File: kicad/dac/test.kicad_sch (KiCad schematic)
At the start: 9 parts, among them U1 PCM2704/4C/5/5C, Y1 12MHz±0.05%

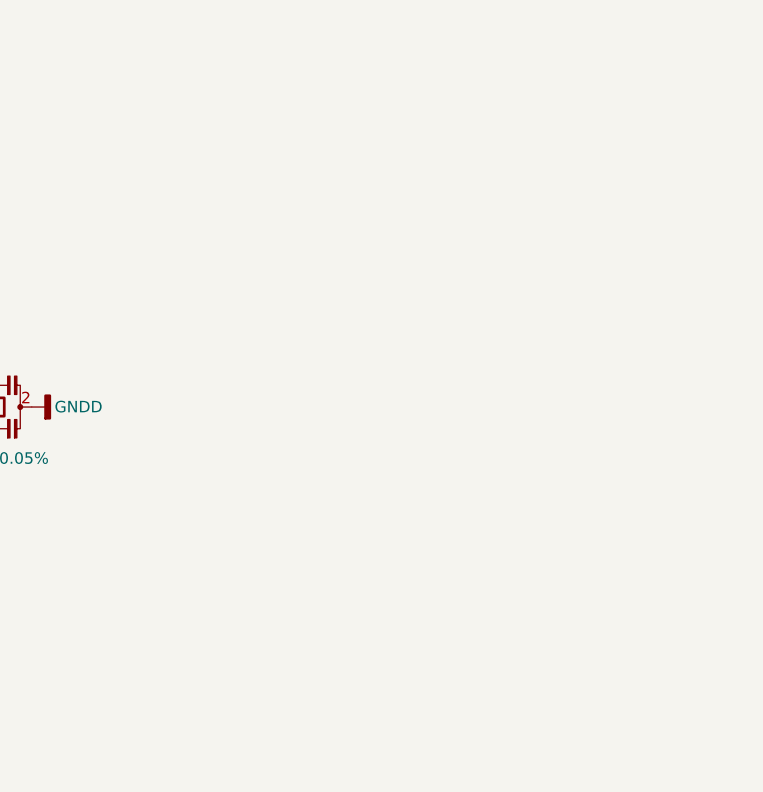
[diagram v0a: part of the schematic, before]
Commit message: completed power supply footprints and placement
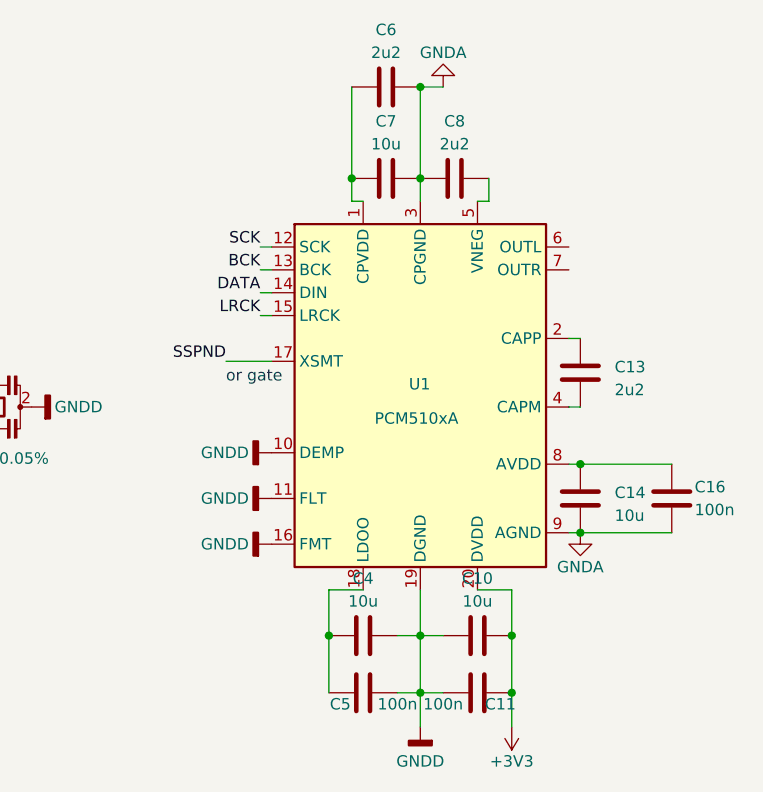
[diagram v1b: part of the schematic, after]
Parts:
- added C10, C14, C4, C7: 10u, Capacitor_SMD:C_1206_3216Metric_Pad1.33x1.80mm_HandSolder, symbol Device:C
- added C11, C16, C5: 100n, Capacitor_SMD:C_1206_3216Metric_Pad1.33x1.80mm_HandSolder, symbol Device:C
- added C13, C6, C8: 2u2, Capacitor_SMD:C_1206_3216Metric_Pad1.33x1.80mm_HandSolder, symbol Device:C
- added U1: PCM510xA, Package_SO:TSSOP-20_4.4x6.5mm_P0.65mm, symbol library:PCM510xA
- C2, C3, C4, C5, C6, R13, R14, U1, Y1: now left out of the parts list
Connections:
- net GNDA: now also C14.2, C16.2, C6.2, C7.2, C8.1, U1.3 (CPGND), U1.9 (AGND)
- net GNDD: now also C10.1, C11.1, C4.2, C5.1, U1.10 (DEMP), U1.11 (FLT), U1.16 (FMT), U1.19 (DGND)
- new net: C6.1, C7.1, U1.1 (CPVDD)
- new net: C4.1, C5.2, U1.18 (LDOO)
- new net: C13.1, U1.2 (CAPP)
- new net: C13.2, U1.4 (CAPM)
- new net: C14.1, C16.1, U1.8 (AVDD)
- new net: C8.2, U1.5 (VNEG)
- new net +3V3: C10.2, C11.2, U1.20 (DVDD)
- new net BCK: U1.13 (BCK)
- new net DATA: U1.14 (DIN)
- new net LRCK: U1.15 (LRCK)
- new net SCK: U1.12 (SCK)
- new net SSPND: U1.17 (XSMT)
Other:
- note added: "or gate"
- company: (none) -> Author: Jona Heinke
- title: (none) -> Test

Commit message: commit
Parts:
- added C34: 10u, symbol Device:C
- added Q11: MMBT5401, Package_TO_SOT_SMD:SOT-23-3, symbol Device:Q_PNP_BEC
- added Q6: MMBT5551, Package_TO_SOT_SMD:SOT-23-3, symbol Device:Q_NPN_BEC
- C10, C11, C13, C14, C16, C2, C3, C4, C5, C6, C7, C8, R13, R14, U1, Y1: now not fitted
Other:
- note added: "cap sizes left to buy: 33p etc. 1u 3u3 good 3u3 470u 2m2"

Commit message: commit
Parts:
- added J4: AudioJack3, symbol Connector_Audio:AudioJack3_Switch
- renumbered C34 to C35
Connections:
- no-connect marks 3 -> 9
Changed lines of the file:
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@@
   (title_block
     (title "Test")
-    (date "2023-05-25")
+    (date "2023-06-03")
     (rev "1")
     (company "Author: Jona Heinke")
@@
   )
   (no_connect (at 36.83 52.07))
+  (no_connect (at 127 127))
   (no_connect (at 72.39 46.99))
+  (no_connect (at 127 121.92))
+  (no_connect (at 127 134.62))
+  (no_connect (at 127 124.46))
+  (no_connect (at 127 129.54))
+  (no_connect (at 127 132.08))
   (no_connect (at 36.83 44.45))
   (wire (pts (xy 31.75 46.99) (xy 36.83 46.99))
@@
         )
         (path "/8a133d32-893e-4939-a0f4-ae81724d72bd/9aaf1754-900d-4340-bdec-8cf556dd71c2"
-          (reference "C43") (unit 1)
+          (reference "C44") (unit 1)
         )
       )
@@
         )
         (path "/8a133d32-893e-4939-a0f4-ae81724d72bd/9aaf1754-900d-4340-bdec-8cf556dd71c2"
-          (reference "C42") (unit 1)
+          (reference "C43") (unit 1)
         )
       )
@@
         )
         (path "/8a133d32-893e-4939-a0f4-ae81724d72bd/9aaf1754-900d-4340-bdec-8cf556dd71c2"
-          (reference "C39") (unit 1)
+          (reference "C40") (unit 1)
         )
       )
@@
         )
         (path "/8a133d32-893e-4939-a0f4-ae81724d72bd/9aaf1754-900d-4340-bdec-8cf556dd71c2"
-          (reference "C41") (unit 1)
+          (reference "C42") (unit 1)
         )
       )
@@
   (symbol (lib_id "Device:C") (at 25.4 134.62 0) (unit 1)
     (in_bom yes) (on_board yes) (dnp no) (fields_autoplaced)
-    (property "Reference" "C34" (at 29.21 133.985 0)
+    (property "Reference" "C35" (at 29.21 133.985 0)
       (effects (font (size 1.27 1.27)) (justify left))
     )
@@
       (project "dac"
         (path "/8a133d32-893e-4939-a0f4-ae81724d72bd/9aaf1754-900d-4340-bdec-8cf556dd71c2"
-          (reference "C34") (unit 1)
+          (reference "C35") (unit 1)
         )
       )
@@
         )
         (path "/8a133d32-893e-4939-a0f4-ae81724d72bd/9aaf1754-900d-4340-bdec-8cf556dd71c2"
-          (reference "C36") (unit 1)
+          (reference "C37") (unit 1)
         )
       )
@@
         )
         (path "/8a133d32-893e-4939-a0f4-ae81724d72bd/9aaf1754-900d-4340-bdec-8cf556dd71c2"
-          (reference "C47") (unit 1)
+          (reference "C48") (unit 1)
         )
       )
@@
         )
         (path "/8a133d32-893e-4939-a0f4-ae81724d72bd/9aaf1754-900d-4340-bdec-8cf556dd71c2"
-          (reference "C38") (unit 1)
+          (reference "C39") (unit 1)
         )
       )
@@
         )
         (path "/8a133d32-893e-4939-a0f4-ae81724d72bd/9aaf1754-900d-4340-bdec-8cf556dd71c2"
-          (reference "C35") (unit 1)
+          (reference "C36") (unit 1)
         )
       )
@@
         )
         (path "/8a133d32-893e-4939-a0f4-ae81724d72bd/9aaf1754-900d-4340-bdec-8cf556dd71c2"
-          (reference "C48") (unit 1)
+          (reference "C49") (unit 1)
         )
       )
@@
     )
   )
+  (symbol (lib_id "Connector_Audio:AudioJack3_Switch") (at 132.08 129.54 180) (unit 1)
+    (in_bom no) (on_board no) (dnp yes)
+    (property "Reference" "J4" (at 132.08 140.97 0)
+      (effects (font (size 1.27 1.27)))
+    )
+    (property "Value" "AudioJack3" (at 132.08 138.43 0)
+      (effects (font (size 1.27 1.27)))
+    )
+    (property "Footprint" "" (at 132.08 129.54 0)
+      (effects (font (size 1.27 1.27)) hide)
+    )
+    (property "Datasheet" "https://www.cuidevices.com/product/resource/sj-6307.pdf" (at 132.08 129.54 0)
+      (effects (font (size 1.27 1.27)) hide)
+    )
+    (property "Digikey" "2223-SJ-63073E-ND" (at 132.08 129.54 0)
+      (effects (font (size 1.27 1.27)) hide)
+    )
+    (pin "R")
+    (pin "RN")
+    (pin "S")
+    (pin "SN")
+    (pin "T")
+    (pin "TN")
+    (instances
+      (project "dac"
+        (path "/8a133d32-893e-4939-a0f4-ae81724d72bd"
+          (reference "J4") (unit 1)
+        )
+        (path "/8a133d32-893e-4939-a0f4-ae81724d72bd/9aaf1754-900d-4340-bdec-8cf556dd71c2"
+          (reference "J5") (unit 1)
+        )
+      )
+    )
+  )
   (symbol (lib_id "Device:R") (at 31.75 38.1 180) (unit 1)
     (in_bom no) (on_board no) (dnp yes) (fields_autoplaced)
@@
         )
         (path "/8a133d32-893e-4939-a0f4-ae81724d72bd/9aaf1754-900d-4340-bdec-8cf556dd71c2"
-          (reference "R61") (unit 1)
+          (reference "R65") (unit 1)
         )
       )
@@
         )
         (path "/8a133d32-893e-4939-a0f4-ae81724d72bd/9aaf1754-900d-4340-bdec-8cf556dd71c2"
-          (reference "C46") (unit 1)
+          (reference "C47") (unit 1)
         )
       )
@@
         )
         (path "/8a133d32-893e-4939-a0f4-ae81724d72bd/9aaf1754-900d-4340-bdec-8cf556dd71c2"
-          (reference "C49") (unit 1)
+          (reference "C50") (unit 1)
         )
       )
@@
         )
         (path "/8a133d32-893e-4939-a0f4-ae81724d72bd/9aaf1754-900d-4340-bdec-8cf556dd71c2"
-          (reference "C40") (unit 1)
+          (reference "C41") (unit 1)
         )
       )
@@
         )
         (path "/8a133d32-893e-4939-a0f4-ae81724d72bd/9aaf1754-900d-4340-bdec-8cf556dd71c2"
-          (reference "C44") (unit 1)
+          (reference "C45") (unit 1)
         )
       )
@@
         )
         (path "/8a133d32-893e-4939-a0f4-ae81724d72bd/9aaf1754-900d-4340-bdec-8cf556dd71c2"
-          (reference "R62") (unit 1)
+          (reference "R66") (unit 1)
         )
       )
@@
         )
         (path "/8a133d32-893e-4939-a0f4-ae81724d72bd/9aaf1754-900d-4340-bdec-8cf556dd71c2"
-          (reference "C45") (unit 1)
+          (reference "C46") (unit 1)
         )
       )
@@
         )
         (path "/8a133d32-893e-4939-a0f4-ae81724d72bd/9aaf1754-900d-4340-bdec-8cf556dd71c2"
-          (reference "C37") (unit 1)
-        )
-      )
+          (reference "C38") (unit 1)
+        )
+      )
